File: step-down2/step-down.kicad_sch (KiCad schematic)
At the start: 22 parts, among them IC1 LTC3807EFE#PBF, J1 Screw_Terminal_01x02, J2 Screw_Terminal_01x02, M1 IRF7413ZPBF, M2 IRF7413ZPBF

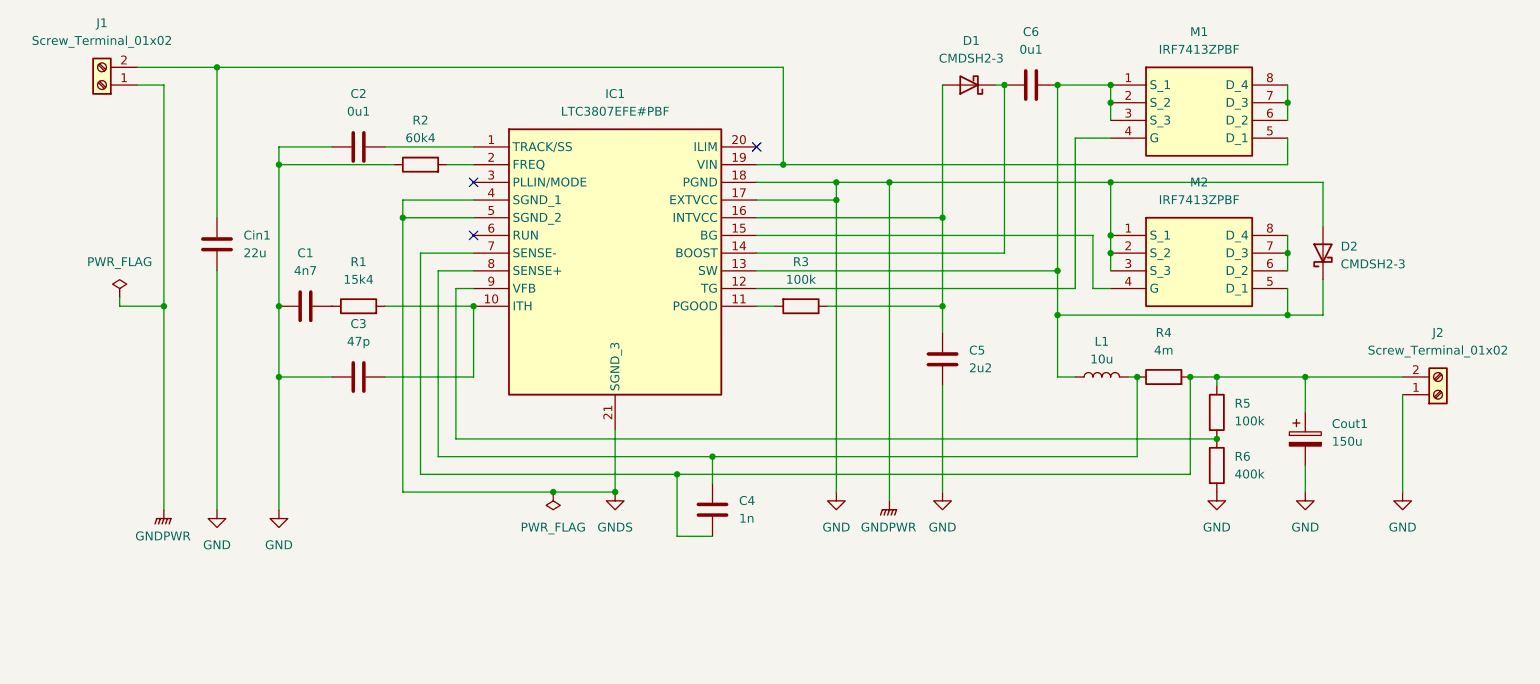
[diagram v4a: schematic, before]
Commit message: fixed all ERC errors
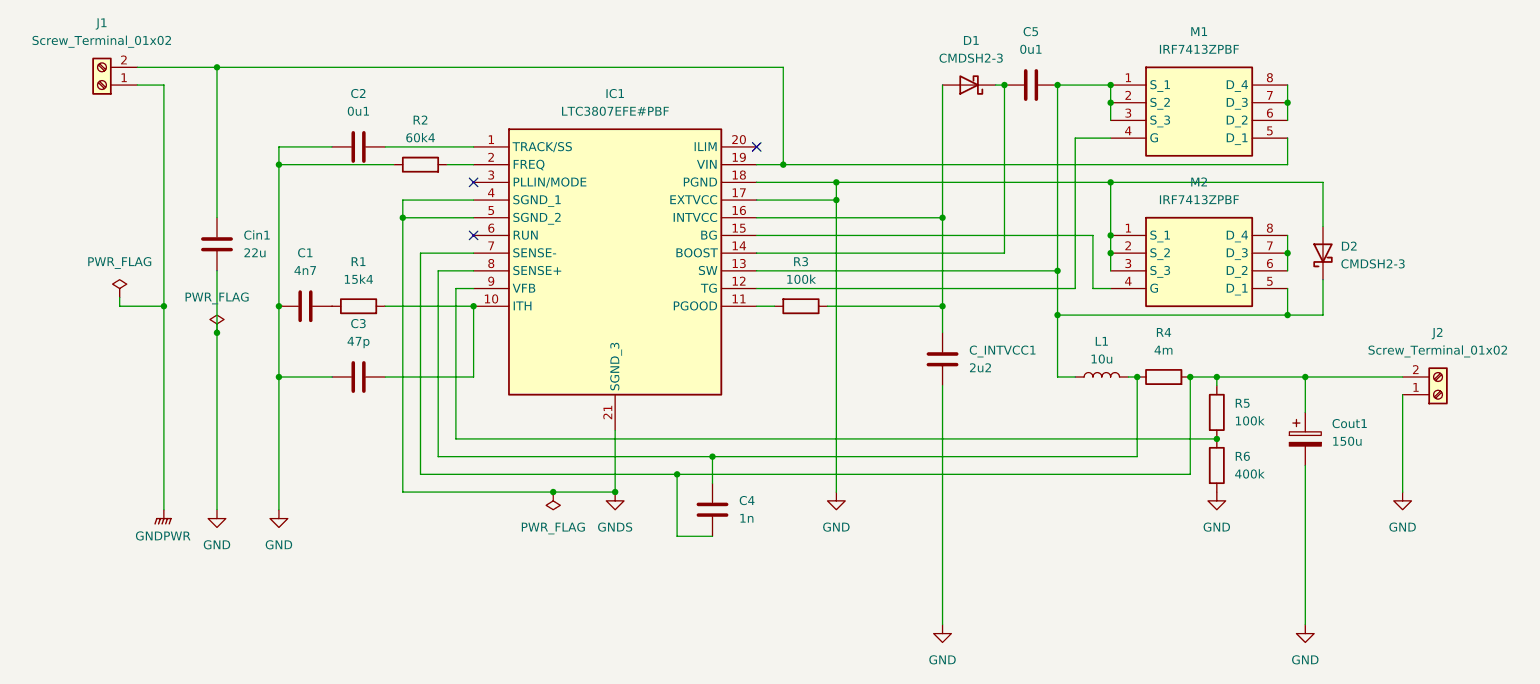
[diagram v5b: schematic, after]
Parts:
- renumbered C6 to C5, C5 to C_INTVCC1
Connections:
- net GND: no longer J1.1 (Pin_1)
- new net GNDPWR: J1.1 (Pin_1)
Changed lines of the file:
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@@
 	)
 	(junction
+		(at 74.93 104.14)
+		(diameter 0)
+		(color 0 0 0 0)
+	)
+	(junction
 		(at 195.58 68.58)
 		(diameter 0)
@@
 	)
 	(junction
-		(at 171.45 82.55)
-		(diameter 0)
-		(color 0 0 0 0)
-	)
-	(junction
 		(at 207.01 110.49)
 		(diameter 0)
@@
 	(wire
 		(pts
-			(xy 231.14 123.19) (xy 231.14 127)
+			(xy 231.14 123.19) (xy 231.14 146.05)
 		)
 		(stroke
@@
 	(wire
 		(pts
-			(xy 179.07 111.76) (xy 179.07 127)
+			(xy 179.07 111.76) (xy 179.07 146.05)
 		)
 		(stroke
@@
 	(wire
 		(pts
-			(xy 74.93 95.25) (xy 74.93 129.54)
+			(xy 74.93 95.25) (xy 74.93 104.14)
 		)
 		(stroke
@@
 	(wire
 		(pts
-			(xy 171.45 82.55) (xy 203.2 82.55)
+			(xy 163.83 82.55) (xy 203.2 82.55)
 		)
 		(stroke
@@
 	(wire
 		(pts
-			(xy 74.93 66.04) (xy 156.21 66.04)
+			(xy 74.93 104.14) (xy 74.93 129.54)
 		)
 		(stroke
@@
 	(wire
 		(pts
-			(xy 163.83 82.55) (xy 171.45 82.55)
+			(xy 74.93 66.04) (xy 156.21 66.04)
 		)
 		(stroke
@@
 	(wire
 		(pts
-			(xy 171.45 82.55) (xy 171.45 128.27)
-		)
-		(stroke
-			(width 0)
-			(type default)
-		)
-	)
-	(wire
-		(pts
 			(xy 140.97 133.35) (xy 146.05 133.35)
 		)
@@
 	)
 	(symbol
-		(lib_id "power:GNDPWR")
-		(at 171.45 128.27 0)
-		(unit 1)
-		(exclude_from_sim no)
-		(in_bom yes)
-		(on_board yes)
-		(dnp no)
-		(fields_autoplaced yes)
-		(property "Reference" "#PWR06"
-			(at 171.45 133.35 0)
-			(effects
-				(font
-					(size 1.27 1.27)
-				)
-				(hide yes)
-			)
-		)
-		(property "Value" "GNDPWR"
-			(at 171.323 132.08 0)
-			(effects
-				(font
-					(size 1.27 1.27)
-				)
-			)
-		)
-		(property "Footprint" ""
-			(at 171.45 129.54 0)
-			(effects
-				(font
-					(size 1.27 1.27)
-				)
-				(hide yes)
-			)
-		)
-		(property "Datasheet" ""
-			(at 171.45 129.54 0)
-			(effects
-				(font
-					(size 1.27 1.27)
-				)
-				(hide yes)
-			)
-		)
-		(property "Description" "Power symbol creates a global label with name \"GNDPWR\" , global ground"
-			(at 171.45 128.27 0)
-			(effects
-				(font
-					(size 1.27 1.27)
-				)
-				(hide yes)
-			)
-		)
-		(pin "1"
-		)
-		(instances
-			(project ""
-				(path "/270a0c1d-99e0-47c8-a788-488ffbf33d34"
-					(reference "#PWR06")
-					(unit 1)
-				)
-			)
-		)
-	)
-	(symbol
 		(lib_id "Device:C")
 		(at 87.63 100.33 90)
@@
 		(dnp no)
 		(fields_autoplaced yes)
-		(property "Reference" "C6"
+		(property "Reference" "C5"
 			(at 191.77 60.96 90)
 			(effects
@@
 			(project ""
 				(path "/270a0c1d-99e0-47c8-a788-488ffbf33d34"
-					(reference "C6")
+					(reference "C5")
 					(unit 1)
 				)
@@
 		(dnp no)
 		(fields_autoplaced yes)
-		(property "Reference" "C5"
+		(property "Reference" "C_INTVCC1"
 			(at 182.88 106.6799 0)
 			(effects
@@
 			(project ""
 				(path "/270a0c1d-99e0-47c8-a788-488ffbf33d34"
-					(reference "C5")
+					(reference "C_INTVCC1")
 					(unit 1)
 				)
@@
 	(symbol
 		(lib_id "power:GND")
-		(at 179.07 127 0)
+		(at 179.07 146.05 0)
 		(unit 1)
 		(exclude_from_sim no)
@@
 		(dnp no)
 		(fields_autoplaced yes)
-		(property "Reference" "#PWR07"
-			(at 179.07 133.35 0)
+		(property "Reference" "#PWR06"
+			(at 179.07 152.4 0)
 			(effects
 				(font
@@
 		)
 		(property "Value" "GND"
-			(at 179.07 132.08 0)
+			(at 179.07 151.13 0)
 			(effects
 				(font
@@
 		)
 		(property "Footprint" ""
-			(at 179.07 127 0)
+			(at 179.07 146.05 0)
 			(effects
 				(font
@@
 		)
 		(property "Datasheet" ""
-			(at 179.07 127 0)
+			(at 179.07 146.05 0)
 			(effects
 				(font
@@
 		)
 		(property "Description" "Power symbol creates a global label with name \"GND\" , ground"
-			(at 179.07 127 0)
+			(at 179.07 146.05 0)
 			(effects
 				(font
@@
 			(project ""
 				(path "/270a0c1d-99e0-47c8-a788-488ffbf33d34"
-					(reference "#PWR07")
+					(reference "#PWR06")
 					(unit 1)
 				)
@@
 		(dnp no)
 		(fields_autoplaced yes)
-		(property "Reference" "#PWR08"
+		(property "Reference" "#PWR07"
 			(at 218.44 133.35 0)
 			(effects
@@
 			(project ""
 				(path "/270a0c1d-99e0-47c8-a788-488ffbf33d34"
-					(reference "#PWR08")
+					(reference "#PWR07")
 					(unit 1)
 				)
@@
 	(symbol
 		(lib_id "power:GND")
-		(at 231.14 127 0)
+		(at 231.14 146.05 0)
 		(unit 1)
 		(exclude_from_sim no)
@@
 		(dnp no)
 		(fields_autoplaced yes)
-		(property "Reference" "#PWR010"
-			(at 231.14 133.35 0)
+		(property "Reference" "#PWR08"
+			(at 231.14 152.4 0)
 			(effects
 				(font
@@
 		)
 		(property "Value" "GND"
-			(at 231.14 132.08 0)
+			(at 231.14 151.13 0)
 			(effects
 				(font
@@
 		)
 		(property "Footprint" ""
-			(at 231.14 127 0)
+			(at 231.14 146.05 0)
 			(effects
 				(font
@@
 		)
 		(property "Datasheet" ""
-			(at 231.14 127 0)
+			(at 231.14 146.05 0)
 			(effects
 				(font
@@
 		)
 		(property "Description" "Power symbol creates a global label with name \"GND\" , ground"
-			(at 231.14 127 0)
+			(at 231.14 146.05 0)
 			(effects
 				(font
@@
 			(project ""
 				(path "/270a0c1d-99e0-47c8-a788-488ffbf33d34"
-					(reference "#PWR010")
+					(reference "#PWR08")
 					(unit 1)
 				)
@@
 		(dnp no)
 		(fields_autoplaced yes)
-		(property "Reference" "#FLG02"
+		(property "Reference" "#FLG03"
 			(at 123.19 128.905 0)
 			(effects
@@
 			(project ""
 				(path "/270a0c1d-99e0-47c8-a788-488ffbf33d34"
-					(reference "#FLG02")
+					(reference "#FLG03")
 					(unit 1)
 				)
@@
 					(unit 1)
 				)
+			)
+		)
+	)
+	(symbol
+		(lib_id "power:PWR_FLAG")
+		(at 74.93 104.14 0)
+		(unit 1)
+		(exclude_from_sim no)
+		(in_bom yes)
+		(on_board yes)
+		(dnp no)
+		(fields_autoplaced yes)
+		(property "Reference" "#FLG02"
+			(at 74.93 102.235 0)
+			(effects
+				(font
+					(size 1.27 1.27)
+				)
+				(hide yes)
+			)
+		)
+		(property "Value" "PWR_FLAG"
+			(at 74.93 99.06 0)
+			(effects
+				(font
+					(size 1.27 1.27)
+				)
+			)
+		)
+		(property "Footprint" ""
+			(at 74.93 104.14 0)
+			(effects
+				(font
+					(size 1.27 1.27)
+				)
+				(hide yes)
+			)
+		)
+		(property "Datasheet" "~"
+			(at 74.93 104.14 0)
+			(effects
+				(font
+					(size 1.27 1.27)
+				)
+				(hide yes)
+			)
+		)
+		(property "Description" "Special symbol for telling ERC where power comes from"
+			(at 74.93 104.14 0)
+			(effects
+				(font
+					(size 1.27 1.27)
+				)
+				(hide yes)
+			)
+		)
+		(pin "1"
+		)
+		(instances
+			(project "step-down"
+				(path "/270a0c1d-99e0-47c8-a788-488ffbf33d34"
+					(reference "#FLG02")
+					(unit 1)
+				)

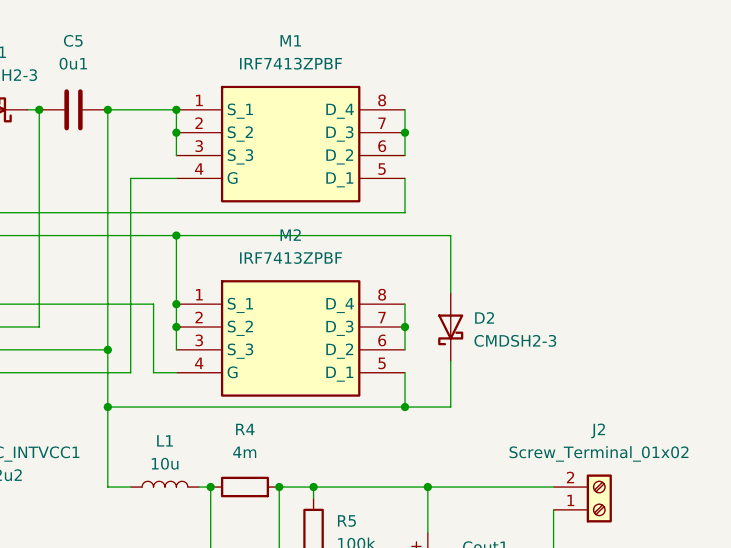
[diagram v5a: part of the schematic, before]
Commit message: fixed all ERC errors
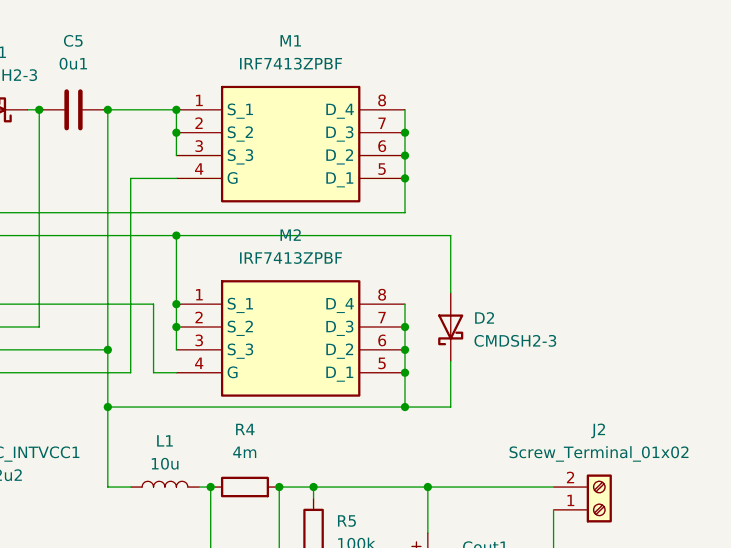
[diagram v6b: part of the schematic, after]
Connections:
- net at C5.2, D2.1 (K), IC1.13 (SW)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: now also M2.6 (D_2), M2.7 (D_3), M2.8 (D_4)
- net at Cin1.1, IC1.19 (VIN), J1.2 (Pin_2)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: now also M1.6 (D_2), M1.7 (D_3), M1.8 (D_4)
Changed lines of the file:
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@@
+	)
+	(junction
+		(at 228.6 73.66)
+		(diameter 0)
+		(color 0 0 0 0)
 	)
 	(junction
@@
 	)
 	(junction
+		(at 228.6 95.25)
+		(diameter 0)
+		(color 0 0 0 0)
+	)
+	(junction
 		(at 179.07 87.63)
 		(diameter 0)
@@
 	(junction
 		(at 146.05 121.92)
+		(diameter 0)
+		(color 0 0 0 0)
+	)
+	(junction
+		(at 228.6 76.2)
+		(diameter 0)
+		(color 0 0 0 0)
+	)
+	(junction
+		(at 228.6 97.79)
 		(diameter 0)
 		(color 0 0 0 0)
@@
 	(wire
 		(pts
+			(xy 228.6 95.25) (xy 228.6 97.79)
+		)
+		(stroke
+			(width 0)
+			(type default)
+		)
+	)
+	(wire
+		(pts
 			(xy 140.97 124.46) (xy 214.63 124.46)
 		)
@@
 		)
 		(stroke
+			(width 0)
+			(type default)
+		)
+	)
+	(wire
+		(pts
+			(xy 228.6 73.66) (xy 228.6 76.2)
+		)
+		(stroke
